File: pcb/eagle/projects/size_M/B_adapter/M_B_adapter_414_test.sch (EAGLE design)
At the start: 13 parts

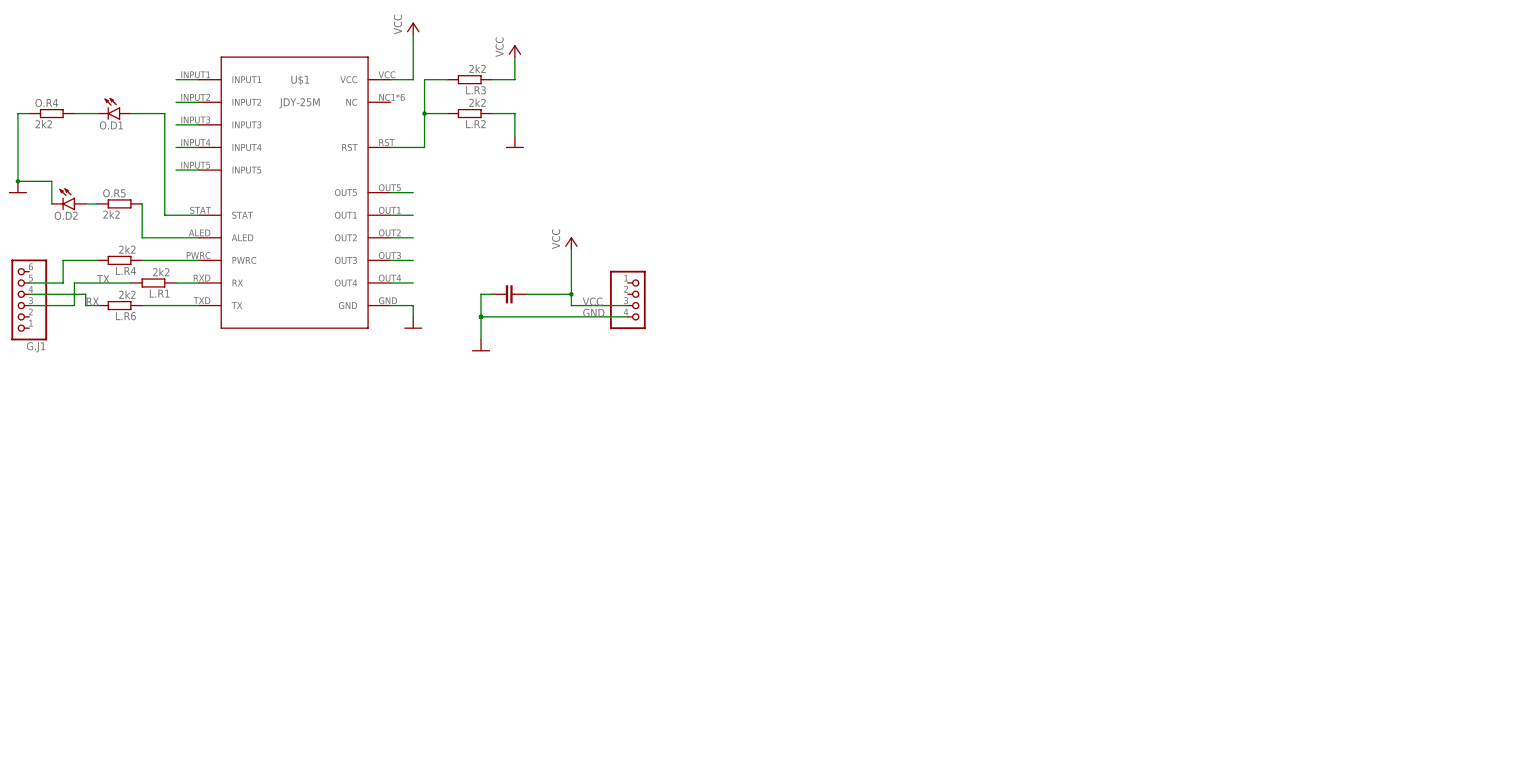
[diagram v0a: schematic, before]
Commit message: reorganized pcb folders
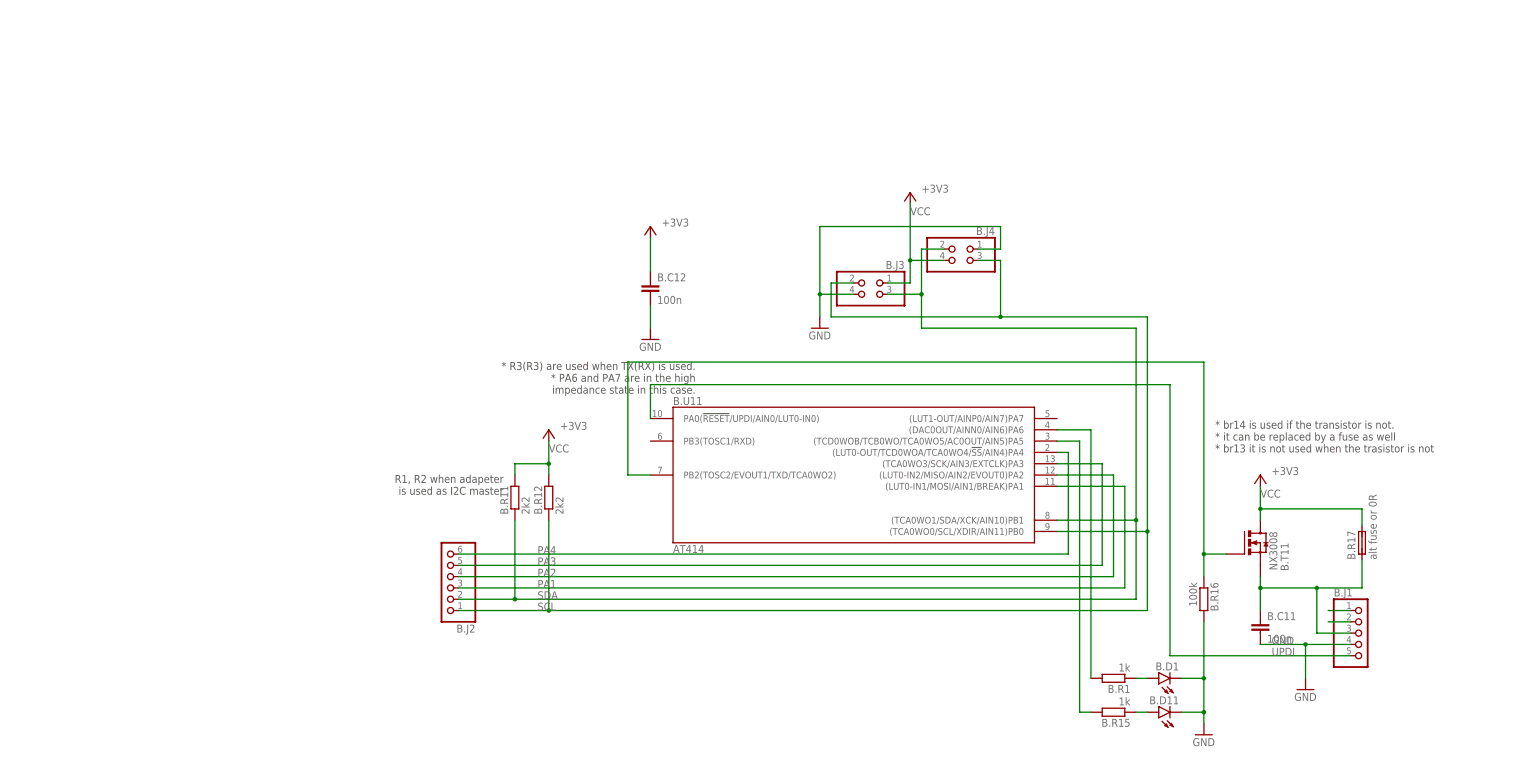
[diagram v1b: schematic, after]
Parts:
- removed G.J1: (no value), pinhead2:PINHD-1X6
- removed G.J2: (no value), pinhead2:PINHD-1X4
- removed L.C1: 100n, rcl:C-EUC0603
- removed L.R1, L.R2, L.R3, L.R4, L.R6, O.R4, O.R5: 2k2, rcl:R-EU_R0603
- removed O.D1, O.D2: (no value), led:LEDCHIP-LED0603
- removed U$1: JDY-25, hugo:JDY-25
- added B.C11, B.C12: 100n, rcl:C-EUC0603
- added B.D1, B.D11: (no value), led:LEDCHIP-LED0603
- added B.J1: (no value), pinhead2:PINHD-1X5
- added B.J2: (no value), pinhead2:PINHD-1X6
- added B.J3, B.J4: (no value), pinhead2:PINHD-2X2
- added B.R1, B.R15: 1k, rcl:R-EU_R0603
- added B.R11, B.R12: 2k2, rcl:R-EU_R0603
- added B.R16: 100k, rcl:R-EU_R0603
- added B.R17: alt fuse or 0R, hugo:FUSE
- added B.T11: NX3008, hugo:N-MOSFET
- added B.U11: AT414, atmel:ATTINY414-SSN
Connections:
- removed net N$1: L.R1.1, U$1.RX
- removed net N$10: O.D2.A, O.R5.1
- removed net N$11: U$1.INPUT2
- removed net N$12: U$1.INPUT3
- removed net N$13: U$1.INPUT4
- removed net N$14: U$1.INPUT5
- removed net N$15: U$1.OUT5
- removed net N$16: U$1.OUT1
- removed net N$17: U$1.OUT2
- removed net N$18: U$1.OUT3
- removed net N$19: U$1.OUT4
- removed net N$2: L.R6.1, U$1.TX
- removed net N$5: L.R2.2, L.R3.2, U$1.RST
- removed net N$6: O.R5.2, U$1.ALED
- removed net N$7: O.D1.A, U$1.STAT
- removed net N$8: U$1.INPUT1
- removed net N$9: O.D1.C, O.R4.2
- removed net RX: G.J1.4, L.R6.2
- removed net TX: G.J1.3, L.R1.2
- new net PA1: B.J2.3, B.U11G$1.(LUT0-IN1/MOSI/AIN1/BREAK)PA1
- new net PA2: B.J2.4, B.U11G$1.(LUT0-IN2/MISO/AIN2/EVOUT0)PA2
- new net PA3: B.J2.5, B.U11G$1.(TCA0WO3/SCK/AIN3/EXTCLK)PA3
- new net PA4: B.J2.6, B.U11G$1.(LUT0-OUT/TCD0WOA/TCA0WO4/!SS!/AIN4)PA4
- new net PA5: B.R15.2, B.U11G$1.(TCD0WOB/TCB0WO/TCA0WO5/AC0OUT/AIN5)PA5
- new net PA51: B.D11.A, B.R15.1
- new net PA6: B.R1.2, B.U11G$1.(DAC0OUT/AINN0/AIN6)PA6
- new net PB2: B.R16.1, B.T11.G, B.U11G$1.PB2(TOSC2/EVOUT1/TXD/TCA0WO2)
- new net SCL: B.J2.1, B.J3.2, B.J4.3, B.R12.1, B.U11G$1.(TCA0WO0/SCL/XDIR/AIN11)PB0
- new net SDA: B.J2.2, B.J3.3, B.J4.2, B.R11.1, B.U11G$1.(TCA0WO1/SDA/XCK/AIN10)PB1
- new net UPDI: B.J1.5, B.U11G$1.PA0(!RESET!/UPDI/AIN0/LUT0-IN0)
- new net VBAT: B.J1.2
- new net VUSB: B.J1.1
- net GND: now also B.C11.2, B.C12.2, B.D1.C, B.D11.C, B.J1.4, B.J3.4, B.J4.1, B.R16.2; no longer G.J2.4, L.C1.1, L.R2.1, O.D2.C, O.R4.1, U$1.GND
- net N$3: now also B.D1.A, B.R1.1; no longer G.J1.5, L.R4.2
- net N$4: now also B.C11.1, B.J1.3, B.R17.1, B.T11.S; no longer L.R4.1, U$1.PWRC
- net VCC: now also B.C12.1, B.J3.1, B.J4.4, B.R11.2, B.R12.2, B.R17.2, B.T11.D; no longer G.J2.3, L.C1.2, L.R3.1, U$1.VCC
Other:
- note added: "* R3(R3) are used when TX(RX) is used. * PA6 and PA7 are in the high impedance state in this case."
- note added: "* br14 is used if the transistor is not. * it can be replaced by a fuse as well * br13 it is not used when the trasistor is not"
- note added: "R1, R2 when adapeter is used as I2C master"
